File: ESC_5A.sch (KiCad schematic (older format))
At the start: 26 parts, among them IC1 EEPROM, IC2 3.3V Reg, IC3 5V_Reg, IC4 ATSAMD21E17D-AUT, J1 USBc, J2 5V_PWR

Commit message: Layout Rev_One done pre review
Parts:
- added Z1: SZMMSZ4713T1G, SOD3716X135N, symbol SamacSys_Parts:SZMMSZ4713T1G
- gave numbers to parts that had none: 1
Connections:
- net +3V3: now also C8.1, C9.1
- net GND: no longer C8.1, C9.1
- net PWR_IN: now also Z1.2; no longer C3.1, IC3.1 (VIN)
- new net PWR: C3.1, IC3.1 (VIN), Z1.1
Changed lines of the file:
@@
 $EndComp
-$Comp
-L power:GND #PWR024
-U 1 1 60D06FC2
-P 8550 3850
-F 0 "#PWR024" H 8550 3600 50  0001 C CNN
-F 1 "GND" H 8555 3677 50  0000 C CNN
-F 2 "" H 8550 3850 50  0001 C CNN
-F 3 "" H 8550 3850 50  0001 C CNN
-	1    8550 3850
-	1    0    0    -1
-$EndComp
-Wire Wire Line
-	8550 3750 8550 3850
 $Comp
 L power:GND #PWR023
@@
 L power:GND #PWR025
 U 1 1 60D0D0CF
-P 8750 6150
-F 0 "#PWR025" H 8750 5900 50  0001 C CNN
-F 1 "GND" H 8755 5977 50  0000 C CNN
-F 2 "" H 8750 6150 50  0001 C CNN
-F 3 "" H 8750 6150 50  0001 C CNN
-	1    8750 6150
-	1    0    0    -1
-$EndComp
-Wire Wire Line
-	8750 6050 8750 6150
+P 9150 6150
+F 0 "#PWR025" H 9150 5900 50  0001 C CNN
+F 1 "GND" H 9155 5977 50  0000 C CNN
+F 2 "" H 9150 6150 50  0001 C CNN
+F 3 "" H 9150 6150 50  0001 C CNN
+	1    9150 6150
+	1    0    0    -1
+$EndComp
 Text GLabel 10100 4150 2    50   Input ~ 0
 D+
@@
 Wire Wire Line
 	5050 4450 5050 4550
-Text GLabel 4250 4450 0    50   Input ~ 0
+Text GLabel 5700 2600 0    50   Input ~ 0
 PWR_IN
 Wire Wire Line
@@
 Wire Wire Line
 	9050 5550 8750 5550
-Wire Wire Line
-	9150 5550 9150 6050
-Wire Wire Line
-	9150 6050 8750 6050
 Wire Notes Line
 	11050 6450 11050 2850
@@
 $EndComp
 $Comp
-L Connector:Conn_01x03_Male J?
+L Connector:Conn_01x03_Male J6
 U 1 1 60FBA964
 P 7150 5400
-F 0 "J?" H 7258 5681 50  0000 C CNN
+F 0 "J6" H 7258 5681 50  0000 C CNN
 F 1 "5V_PWR" H 7258 5590 50  0000 C CNN
 F 2 "Connector_PinHeader_2.54mm:PinHeader_1x03_P2.54mm_Vertical" H 7150 5400 50  0001 C CNN
@@
 	7350 5500 7450 5500
 $Comp
-L power:GND #PWR?
+L power:GND #PWR0104
 U 1 1 60FBA96B
 P 7450 5500
-F 0 "#PWR?" H 7450 5250 50  0001 C CNN
+F 0 "#PWR0104" H 7450 5250 50  0001 C CNN
 F 1 "GND" H 7455 5327 50  0000 C CNN
 F 2 "" H 7450 5500 50  0001 C CNN
@@
 $EndComp
 $Comp
-L power:+5V #PWR?
+L power:+5V #PWR0105
 U 1 1 60FBA972
 P 7650 5400
-F 0 "#PWR?" H 7650 5250 50  0001 C CNN
+F 0 "#PWR0105" H 7650 5250 50  0001 C CNN
 F 1 "+5V" H 7665 5573 50  0000 C CNN
 F 2 "" H 7650 5400 50  0001 C CNN
@@
 Wire Wire Line
 	8000 3000 8000 3250
+Wire Wire Line
+	9150 5550 9150 6150
+$Comp
+L power:+3.3V #PWR0106
+U 1 1 60E5850F
+P 8750 6050
+F 0 "#PWR0106" H 8750 5900 50  0001 C CNN
+F 1 "+3.3V" H 8765 6223 50  0000 C CNN
+F 2 "" H 8750 6050 50  0001 C CNN
+F 3 "" H 8750 6050 50  0001 C CNN
+	1    8750 6050
+	-1   0    0    1
+$EndComp
+$Comp
+L power:+3.3V #PWR0107
+U 1 1 60E5C5E8
+P 8550 3750
+F 0 "#PWR0107" H 8550 3600 50  0001 C CNN
+F 1 "+3.3V" H 8565 3923 50  0000 C CNN
+F 2 "" H 8550 3750 50  0001 C CNN
+F 3 "" H 8550 3750 50  0001 C CNN
+	1    8550 3750
+	-1   0    0    1
+$EndComp
+$Comp
+L SamacSys_Parts:SZMMSZ4713T1G Z1
+U 1 1 60EAF0E9
+P 6450 2600
+F 0 "Z1" H 6750 2333 50  0000 C CNN
+F 1 "SZMMSZ4713T1G" H 6750 2424 50  0000 C CNN
+F 2 "SOD3716X135N" H 6850 2750 50  0001 L CNN
+F 3 "https://componentsearchengine.com/Datasheets/2/SZMMSZ4713T1G.pdf" H 6850 2650 50  0001 L CNN
+F 4 "Zener Diodes ZEN REG 0.5W 30V" H 6850 2550 50  0001 L CNN "Description"
+F 5 "1.35" H 6850 2450 50  0001 L CNN "Height"
+F 6 "863-SZMMSZ4713T1G" H 6850 2350 50  0001 L CNN "Mouser Part Number"
+F 7 "https://www.mouser.co.uk/ProductDetail/ON-Semiconductor/SZMMSZ4713T1G?qs=PJJcWtbOkNU%2F%252BcrJAwZPrw%3D%3D" H 6850 2250 50  0001 L CNN "Mouser Price/Stock"
+F 8 "ON Semiconductor" H 6850 2150 50  0001 L CNN "Manufacturer_Name"
+F 9 "SZMMSZ4713T1G" H 6850 2050 50  0001 L CNN "Manufacturer_Part_Number"
+	1    6450 2600
+	-1   0    0    1
+$EndComp
+Wire Wire Line
+	5700 2600 5850 2600
+Wire Wire Line
+	6450 2600 6600 2600
+Text GLabel 6600 2600 2    50   Input ~ 0
+PWR
+Text GLabel 4250 4450 0    50   Input ~ 0
+PWR
 $EndSCHEMATC

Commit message: pre layout
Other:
- note added: "Mounting Hole"
- note added: "Polarity Protection"
- moved on the sheet: H1, H2, Z1
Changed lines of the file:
@@
 Wire Wire Line
 	5050 4450 5050 4550
-Text GLabel 5700 2600 0    50   Input ~ 0
+Text GLabel 5450 2600 0    50   Input ~ 0
 PWR_IN
 Wire Wire Line
@@
 	11050 6450 11050 2850
 Wire Notes Line
-	6900 2850 6900 7750
-Wire Notes Line
 	2150 6450 11050 6450
 Text Notes 7000 2950 0    50   ~ 0
@@
 $EndComp
 Wire Notes Line
-	3750 2850 3750 7750
-Wire Notes Line
 	3750 2850 11050 2850
 Text Notes 3800 2950 0    50   ~ 0
@@
 L Mechanical:MountingHole H2
 U 1 1 60EFB1DF
-P 3850 2650
-F 0 "H2" H 3950 2696 50  0000 L CNN
-F 1 "MountingHole" H 3950 2605 50  0000 L CNN
-F 2 "MountingHole:MountingHole_2.2mm_M2" H 3850 2650 50  0001 C CNN
-F 3 "~" H 3850 2650 50  0001 C CNN
-	1    3850 2650
+P 4050 2550
+F 0 "H2" H 4150 2596 50  0000 L CNN
+F 1 "MountingHole" H 4150 2505 50  0000 L CNN
+F 2 "MountingHole:MountingHole_2.2mm_M2" H 4050 2550 50  0001 C CNN
+F 3 "~" H 4050 2550 50  0001 C CNN
+	1    4050 2550
 	1    0    0    -1
 $EndComp
@@
 L Mechanical:MountingHole H1
 U 1 1 60EFB7EF
-P 3850 2400
-F 0 "H1" H 3950 2446 50  0000 L CNN
-F 1 "MountingHole" H 3950 2355 50  0000 L CNN
-F 2 "MountingHole:MountingHole_2.2mm_M2" H 3850 2400 50  0001 C CNN
-F 3 "~" H 3850 2400 50  0001 C CNN
-	1    3850 2400
+P 4050 2300
+F 0 "H1" H 4150 2346 50  0000 L CNN
+F 1 "MountingHole" H 4150 2255 50  0000 L CNN
+F 2 "MountingHole:MountingHole_2.2mm_M2" H 4050 2300 50  0001 C CNN
+F 3 "~" H 4050 2300 50  0001 C CNN
+	1    4050 2300
 	1    0    0    -1
 $EndComp
@@
 L SamacSys_Parts:SZMMSZ4713T1G Z1
 U 1 1 60EAF0E9
-P 6450 2600
-F 0 "Z1" H 6750 2333 50  0000 C CNN
-F 1 "SZMMSZ4713T1G" H 6750 2424 50  0000 C CNN
-F 2 "SOD3716X135N" H 6850 2750 50  0001 L CNN
-F 3 "https://componentsearchengine.com/Datasheets/2/SZMMSZ4713T1G.pdf" H 6850 2650 50  0001 L CNN
-F 4 "Zener Diodes ZEN REG 0.5W 30V" H 6850 2550 50  0001 L CNN "Description"
-F 5 "1.35" H 6850 2450 50  0001 L CNN "Height"
-F 6 "863-SZMMSZ4713T1G" H 6850 2350 50  0001 L CNN "Mouser Part Number"
-F 7 "https://www.mouser.co.uk/ProductDetail/ON-Semiconductor/SZMMSZ4713T1G?qs=PJJcWtbOkNU%2F%252BcrJAwZPrw%3D%3D" H 6850 2250 50  0001 L CNN "Mouser Price/Stock"
-F 8 "ON Semiconductor" H 6850 2150 50  0001 L CNN "Manufacturer_Name"
-F 9 "SZMMSZ4713T1G" H 6850 2050 50  0001 L CNN "Manufacturer_Part_Number"
-	1    6450 2600
+P 6200 2600
+F 0 "Z1" H 6500 2333 50  0000 C CNN
+F 1 "SZMMSZ4713T1G" H 6500 2424 50  0000 C CNN
+F 2 "SOD3716X135N" H 6600 2750 50  0001 L CNN
+F 3 "https://componentsearchengine.com/Datasheets/2/SZMMSZ4713T1G.pdf" H 6600 2650 50  0001 L CNN
+F 4 "Zener Diodes ZEN REG 0.5W 30V" H 6600 2550 50  0001 L CNN "Description"
+F 5 "1.35" H 6600 2450 50  0001 L CNN "Height"
+F 6 "863-SZMMSZ4713T1G" H 6600 2350 50  0001 L CNN "Mouser Part Number"
+F 7 "https://www.mouser.co.uk/ProductDetail/ON-Semiconductor/SZMMSZ4713T1G?qs=PJJcWtbOkNU%2F%252BcrJAwZPrw%3D%3D" H 6600 2250 50  0001 L CNN "Mouser Price/Stock"
+F 8 "ON Semiconductor" H 6600 2150 50  0001 L CNN "Manufacturer_Name"
+F 9 "SZMMSZ4713T1G" H 6600 2050 50  0001 L CNN "Manufacturer_Part_Number"
+	1    6200 2600
 	-1   0    0    1
 $EndComp
 Wire Wire Line
-	5700 2600 5850 2600
-Wire Wire Line
-	6450 2600 6600 2600
-Text GLabel 6600 2600 2    50   Input ~ 0
+	5450 2600 5600 2600
+Wire Wire Line
+	6200 2600 6350 2600
+Text GLabel 6350 2600 2    50   Input ~ 0
 PWR
 Text GLabel 4250 4450 0    50   Input ~ 0
 PWR
+Wire Notes Line
+	6900 2100 3750 2100
+Wire Notes Line
+	6900 2100 6900 7750
+Wire Notes Line
+	3750 2100 3750 7750
+Wire Notes Line
+	4900 2850 4900 2100
+Text Notes 3850 2800 0    50   ~ 0
+Mounting Hole
+Text Notes 4950 2200 0    50   ~ 0
+Polarity Protection
 $EndSCHEMATC

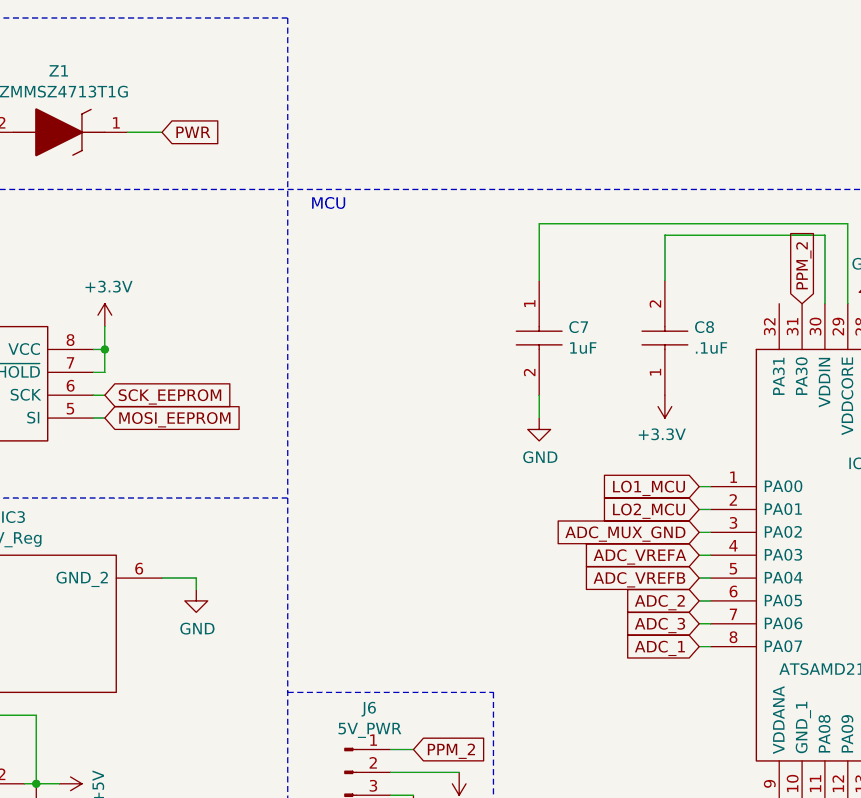
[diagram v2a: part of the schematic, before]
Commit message: removed two current sense resistors and multiple unsused ADC pins
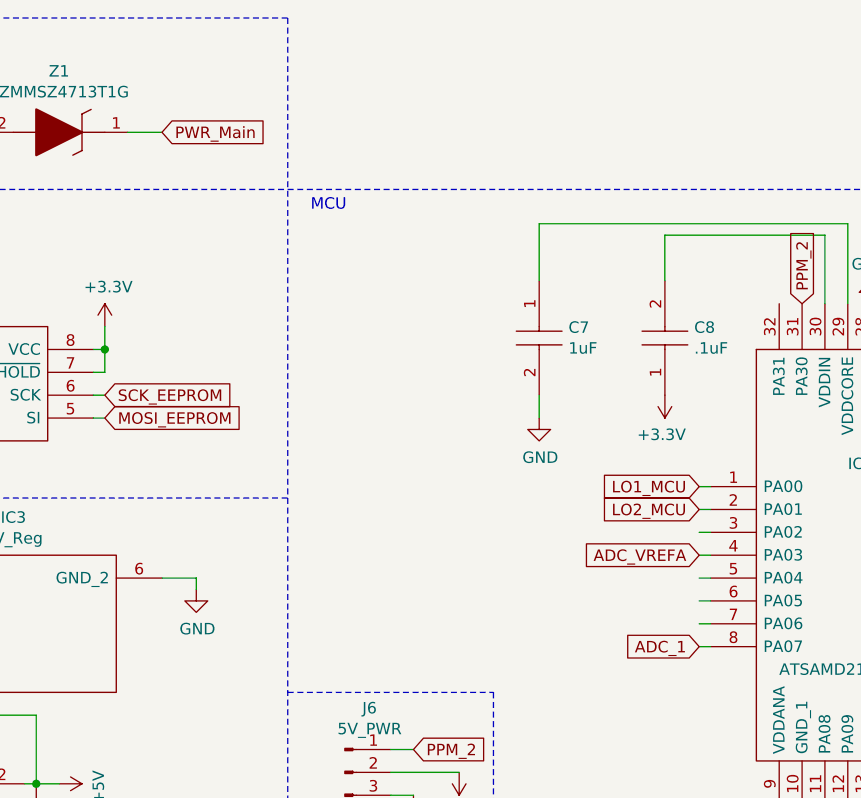
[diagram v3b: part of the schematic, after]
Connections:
- net labels added: PWR_Main
- net labels removed: ADC_2, ADC_3, ADC_MUX_GND, ADC_VREFB
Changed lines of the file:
@@
 Text GLabel 8700 4450 0    50   Input ~ 0
 ADC_VREFA
-Text GLabel 8700 4550 0    50   Input ~ 0
-ADC_VREFB
 Text GLabel 8700 4850 0    50   Input ~ 0
 ADC_1
-Text GLabel 8700 4650 0    50   Input ~ 0
-ADC_2
-Text GLabel 8700 4350 0    50   Input ~ 0
-ADC_MUX_GND
-Text GLabel 8700 4750 0    50   Input ~ 0
-ADC_3
 Wire Wire Line
 	10050 4350 10100 4350
@@
 	6200 2600 6350 2600
 Text GLabel 6350 2600 2    50   Input ~ 0
-PWR
+PWR_Main
 Text GLabel 4250 4450 0    50   Input ~ 0
 PWR

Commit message: Waiting on 4 layer results
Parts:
- removed Z1: SZMMSZ4713T1G, SOD3716X135N, symbol SamacSys_Parts:SZMMSZ4713T1G
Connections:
- net labels added: ADC_2, ADC_3, ADC_MUX_GND, ADC_VREFB
- net labels removed: PWR, PWR_Main
- wire segments 118 -> 119
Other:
- note removed: "Mounting Hole"
- note removed: "Polarity Protection"
- moved on the sheet: H1, H2
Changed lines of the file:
@@
 $EndComp
+$Comp
+L power:GND #PWR024
+U 1 1 60D06FC2
+P 8550 3850
+F 0 "#PWR024" H 8550 3600 50  0001 C CNN
+F 1 "GND" H 8555 3677 50  0000 C CNN
+F 2 "" H 8550 3850 50  0001 C CNN
+F 3 "" H 8550 3850 50  0001 C CNN
+	1    8550 3850
+	1    0    0    -1
+$EndComp
+Wire Wire Line
+	8550 3750 8550 3850
 $Comp
 L power:GND #PWR023
@@
 L power:GND #PWR025
 U 1 1 60D0D0CF
-P 9150 6150
-F 0 "#PWR025" H 9150 5900 50  0001 C CNN
-F 1 "GND" H 9155 5977 50  0000 C CNN
-F 2 "" H 9150 6150 50  0001 C CNN
-F 3 "" H 9150 6150 50  0001 C CNN
-	1    9150 6150
-	1    0    0    -1
-$EndComp
+P 8750 6150
+F 0 "#PWR025" H 8750 5900 50  0001 C CNN
+F 1 "GND" H 8755 5977 50  0000 C CNN
+F 2 "" H 8750 6150 50  0001 C CNN
+F 3 "" H 8750 6150 50  0001 C CNN
+	1    8750 6150
+	1    0    0    -1
+$EndComp
+Wire Wire Line
+	8750 6050 8750 6150
 Text GLabel 10100 4150 2    50   Input ~ 0
 D+
@@
 Wire Wire Line
 	5050 4450 5050 4550
-Text GLabel 5450 2600 0    50   Input ~ 0
+Text GLabel 4250 4450 0    50   Input ~ 0
 PWR_IN
 Wire Wire Line
@@
 Wire Wire Line
 	9050 5550 8750 5550
+Wire Wire Line
+	9150 5550 9150 6050
+Wire Wire Line
+	9150 6050 8750 6050
 Wire Notes Line
 	11050 6450 11050 2850
+Wire Notes Line
+	6900 2850 6900 7750
 Wire Notes Line
 	2150 6450 11050 6450
@@
 Text GLabel 8700 4450 0    50   Input ~ 0
 ADC_VREFA
+Text GLabel 8700 4550 0    50   Input ~ 0
+ADC_VREFB
 Text GLabel 8700 4850 0    50   Input ~ 0
 ADC_1
+Text GLabel 8700 4650 0    50   Input ~ 0
+ADC_2
+Text GLabel 8700 4350 0    50   Input ~ 0
+ADC_MUX_GND
+Text GLabel 8700 4750 0    50   Input ~ 0
+ADC_3
 Wire Wire Line
 	10050 4350 10100 4350
@@
 	1    0    0    -1
 $EndComp
+Wire Notes Line
+	3750 2850 3750 7750
 Wire Notes Line
 	3750 2850 11050 2850
@@
 L Mechanical:MountingHole H2
 U 1 1 60EFB1DF
-P 4050 2550
-F 0 "H2" H 4150 2596 50  0000 L CNN
-F 1 "MountingHole" H 4150 2505 50  0000 L CNN
-F 2 "MountingHole:MountingHole_2.2mm_M2" H 4050 2550 50  0001 C CNN
-F 3 "~" H 4050 2550 50  0001 C CNN
-	1    4050 2550
+P 3850 2650
+F 0 "H2" H 3950 2696 50  0000 L CNN
+F 1 "MountingHole" H 3950 2605 50  0000 L CNN
+F 2 "MountingHole:MountingHole_2.2mm_M2" H 3850 2650 50  0001 C CNN
+F 3 "~" H 3850 2650 50  0001 C CNN
+	1    3850 2650
 	1    0    0    -1
 $EndComp
@@
 L Mechanical:MountingHole H1
 U 1 1 60EFB7EF
-P 4050 2300
-F 0 "H1" H 4150 2346 50  0000 L CNN
-F 1 "MountingHole" H 4150 2255 50  0000 L CNN
-F 2 "MountingHole:MountingHole_2.2mm_M2" H 4050 2300 50  0001 C CNN
-F 3 "~" H 4050 2300 50  0001 C CNN
-	1    4050 2300
+P 3850 2400
+F 0 "H1" H 3950 2446 50  0000 L CNN
+F 1 "MountingHole" H 3950 2355 50  0000 L CNN
+F 2 "MountingHole:MountingHole_2.2mm_M2" H 3850 2400 50  0001 C CNN
+F 3 "~" H 3850 2400 50  0001 C CNN
+	1    3850 2400
 	1    0    0    -1
 $EndComp
@@
 Wire Wire Line
 	8000 3000 8000 3250
-Wire Wire Line
-	9150 5550 9150 6150
-$Comp
-L power:+3.3V #PWR0106
-U 1 1 60E5850F
-P 8750 6050
-F 0 "#PWR0106" H 8750 5900 50  0001 C CNN
-F 1 "+3.3V" H 8765 6223 50  0000 C CNN
-F 2 "" H 8750 6050 50  0001 C CNN
-F 3 "" H 8750 6050 50  0001 C CNN
-	1    8750 6050
-	-1   0    0    1
-$EndComp
-$Comp
-L power:+3.3V #PWR0107
-U 1 1 60E5C5E8
-P 8550 3750
-F 0 "#PWR0107" H 8550 3600 50  0001 C CNN
-F 1 "+3.3V" H 8565 3923 50  0000 C CNN
-F 2 "" H 8550 3750 50  0001 C CNN
-F 3 "" H 8550 3750 50  0001 C CNN
-	1    8550 3750
-	-1   0    0    1
-$EndComp
-$Comp
-L SamacSys_Parts:SZMMSZ4713T1G Z1
-U 1 1 60EAF0E9
-P 6200 2600
-F 0 "Z1" H 6500 2333 50  0000 C CNN
-F 1 "SZMMSZ4713T1G" H 6500 2424 50  0000 C CNN
-F 2 "SOD3716X135N" H 6600 2750 50  0001 L CNN
-F 3 "https://componentsearchengine.com/Datasheets/2/SZMMSZ4713T1G.pdf" H 6600 2650 50  0001 L CNN
-F 4 "Zener Diodes ZEN REG 0.5W 30V" H 6600 2550 50  0001 L CNN "Description"
-F 5 "1.35" H 6600 2450 50  0001 L CNN "Height"
-F 6 "863-SZMMSZ4713T1G" H 6600 2350 50  0001 L CNN "Mouser Part Number"
-F 7 "https://www.mouser.co.uk/ProductDetail/ON-Semiconductor/SZMMSZ4713T1G?qs=PJJcWtbOkNU%2F%252BcrJAwZPrw%3D%3D" H 6600 2250 50  0001 L CNN "Mouser Price/Stock"
-F 8 "ON Semiconductor" H 6600 2150 50  0001 L CNN "Manufacturer_Name"
-F 9 "SZMMSZ4713T1G" H 6600 2050 50  0001 L CNN "Manufacturer_Part_Number"
-	1    6200 2600
-	-1   0    0    1
-$EndComp
-Wire Wire Line
-	5450 2600 5600 2600
-Wire Wire Line
-	6200 2600 6350 2600
-Text GLabel 6350 2600 2    50   Input ~ 0
-PWR_Main
-Text GLabel 4250 4450 0    50   Input ~ 0
-PWR
-Wire Notes Line
-	6900 2100 3750 2100
-Wire Notes Line
-	6900 2100 6900 7750
-Wire Notes Line
-	3750 2100 3750 7750
-Wire Notes Line
-	4900 2850 4900 2100
-Text Notes 3850 2800 0    50   ~ 0
-Mounting Hole
-Text Notes 4950 2200 0    50   ~ 0
-Polarity Protection
 $EndSCHEMATC
